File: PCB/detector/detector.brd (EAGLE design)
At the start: 60 x 60 mm, 20 parts, among them U2 B39431B3710U410, U3 LT5537EDDBTRPBF

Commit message: first connection commit
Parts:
- added C10, C11, C12, C13, C14, C15, C18, C22: 100nF, resistor:C0603
- added C16: 1uF, resistor:C0603
- added C17, C19: 4,7uF, rcl:SMC_A
- added C20, C21: 22pF, resistor:C0603
- added CAN+PWR: 4PIN_3.81_KATOWA, zielone raster 3.81:CON-PHOENIX_3.81-4PIN_KAT
- added DA1: SN65HVD230, can_driver:SO08
- added FUSE1: 3A, resistor:R0603
- added IC1: LM50, linear:SOT23
- added L1: 1uH/500mA, rcl:L2012C
- added L2: 10uH/20mA, rcl:L2012C
- added LED1: zielona, led:CHIP-LED0603
- added LED2: niebieska, led:CHIP-LED0603
- added MA_BYC_ACS711_!!: ACS712, acs712:SO08
- added PROGRAMATOR: (no value), pinhead:1X06
- added Q1: (no value), transistor-power:SO-08
- added R10: ZW 0-100K, resistor:R0603
- added R11: 120R*, resistor:R0603
- added R12, R14, R15: 10k, resistor:R0603
- added R13: 820R, resistor:R0603
- added R16: 470R, resistor:R0603
- added R17, R9: 32k, resistor:R0603
- added R2, R4, R5: (no value), rcl:R0603
- added R8: 100K, resistor:R0603
- added SIGNAL1: (no value), adafruit:SMA_EDGELAUNCH
- added TRANSIL1: 3.3V, diode:SMBJ
- added U$2: STM32F072RBT6, STM32F072RBT6:TQFP64
- added U$3: ABM3, crystal_scorpio:ABM3
- added U$4: D24V22F3, przetwornice:D24V22F3
- added U$6: LC03-6R2G, LC03-6R2 - diody ESD do magistrali:SOIC-8
- added ZW_MASY: (no value), resistor:R0603
- added ZW_ZASILANIA: (no value), pinhead:1X02
- moved C1 8.64 mm to (88.6, 5.40)
- moved R1 8.64 mm to (86.1, 4.38)
- moved L3 8.25 mm to (91.4, 4.38)
- moved C2 8.00 mm to (119.2, 5.41)
- moved C4 8.00 mm to (103.3, 5.40)
- moved C5 8.00 mm to (113.6, 5.40)
- moved C7 8.00 mm to (119.2, 3.30)
- moved R7 8.00 mm to (126.1, 6.81)
- moved U$1 8.00 mm to (107.4, 5.14)
- moved U3 8.00 mm to (122.9, 5.16)
- moved C24 8.00 mm to (105.0, 10.8)
- moved C3 8.00 mm to (94.4, 5.40)
- moved C6 8.00 mm to (107.3, 10.8)
- moved L4 8.00 mm to (110.5, 6.35)
- moved R3 8.00 mm to (115.3, 10.2)
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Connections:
- new net +24V: Q1.1, Q1.2, Q1.3, R15.2, U$4.IN+
- new net AGND: C14.2, C16.2, C17.-, C18.2, IC1.3, MA_BYC_ACS711_!!.5, R9.1, U$2.12, ZW_MASY.2
- new net BOOT_0: PROGRAMATOR.4, R14.2, U$2.60
- new net CANH_1: DA1.7, R11.2, U$6.1
- new net CANL_1: DA1.6, R11.1, U$6.4
- new net CAN_RX_1: DA1.4, U$2.61
- new net CAN_TX_1: DA1.1, U$2.62
- new net LED1_ON: U$2.15
- new net LED2_ON: U$2.16
- new net LED3_ON: U$2.17
- new net N$10: MA_BYC_ACS711_!!.1, MA_BYC_ACS711_!!.2, Q1.5, Q1.6, Q1.7, Q1.8
- new net N$12: R13.1, U$2.6
- new net N$13: C20.1, U$2.5, U$3.P$2
- new net N$14: C14.1, C16.1, C17.+, L2.2, U$2.13
- new net N$15: C21.1, R13.2, U$3.P$4
- new net N$16: CAN+PWR.P$2, U$6.8
- new net N$17: CAN+PWR.P$1, U$6.5
- new net N$18: LED1.A, R15.1
- new net N$19: LED2.A, R16.1
- new net N$20: Q1.4, R17.1
- new net N$24: PROGRAMATOR.2, ZW_ZASILANIA.1
- new net N$4: R2.1, SIGNAL.P
- new net N$6: R4.1, SIGNAL1.P
- new net N$7: MA_BYC_ACS711_!!.7, R8.1
- new net N$8: DA1.8, R10.1
- new net N$9: FUSE1.1, U$4.OUT+
- new net NRST: C22.1, PROGRAMATOR.3, U$2.7
- new net OVER_CURRENT: MA_BYC_ACS711_!!.6, R12.2, U$2.2
- new net PRAD_PLYTKI: R8.2, R9.2, U$2.8
- new net SIGNAL1: R2.2, R4.2, R5.2
- new net SWDIO: PROGRAMATOR.6, U$2.46
- new net SWD_CLK: PROGRAMATOR.5, U$2.49
- new net TEMP: IC1.2, U$2.9
- new net VCC: CAN+PWR.P$4, MA_BYC_ACS711_!!.3, MA_BYC_ACS711_!!.4
- new net VDD: C10.1, C11.1, C12.1, C13.1, C15.2, C18.1, C19.+, DA1.3, IC1.1, L1.1, L2.1, MA_BYC_ACS711_!!.8, R12.1, U$2.19, U$2.32, U$2.48, U$2.64, ZW_ZASILANIA.2
- net +3V3: now also FUSE1.2, L1.2, R16.2, TRANSIL1.C
- net GND: now also C10.2, C11.2, C12.2, C13.2, C15.1, C19.-, C20.2, C21.2, C22.2, CAN+PWR.P$3, DA1.2, LED1.C, LED2.C, PROGRAMATOR.1, R10.2, R14.1, R17.2, SIGNAL1.GND@1, SIGNAL1.GND@2, SIGNAL1.GND@3, SIGNAL1.GND@4, TRANSIL1.A, U$2.18, U$2.31, U$2.47, U$2.63, U$3.P$1, U$3.P$3, U$4.GND, U$4.GND1, U$6.2, U$6.3, U$6.6, U$6.7, ZW_MASY.1
- net SIGNAL: now also R5.1; no longer SIGNAL.P
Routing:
- net GND: track 125.9 -> 410.1 mm, vias 98 -> 163
- net VDD: track 0.00 -> 98.7 mm, vias 0 -> 9
- net VCC: track 0.00 -> 43.0 mm
- net AGND: track 0.00 -> 39.5 mm, vias 0 -> 3
- net OVER_CURRENT: track 0.00 -> 27.0 mm, vias 0 -> 2
- net NRST: track 0.00 -> 26.4 mm, vias 0 -> 1
- net N$16: track 0.00 -> 20.9 mm, vias 0 -> 1
- net N$17: track 0.00 -> 20.4 mm
- net PRAD_PLYTKI: track 0.00 -> 17.4 mm
- net TEMP: track 0.00 -> 16.8 mm, vias 0 -> 1
- net +24V: track 0.00 -> 15.8 mm
- net N$9: track 0.00 -> 15.1 mm
- net BOOT_0: track 0.00 -> 14.9 mm, vias 0 -> 2
- net N$6: track 0.00 -> 11.7 mm
- net N$13: track 0.00 -> 10.4 mm
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- removed copper zone on layer 1, net GND
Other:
- board size 60 x 60 mm -> 134.8 x 62.2 mm

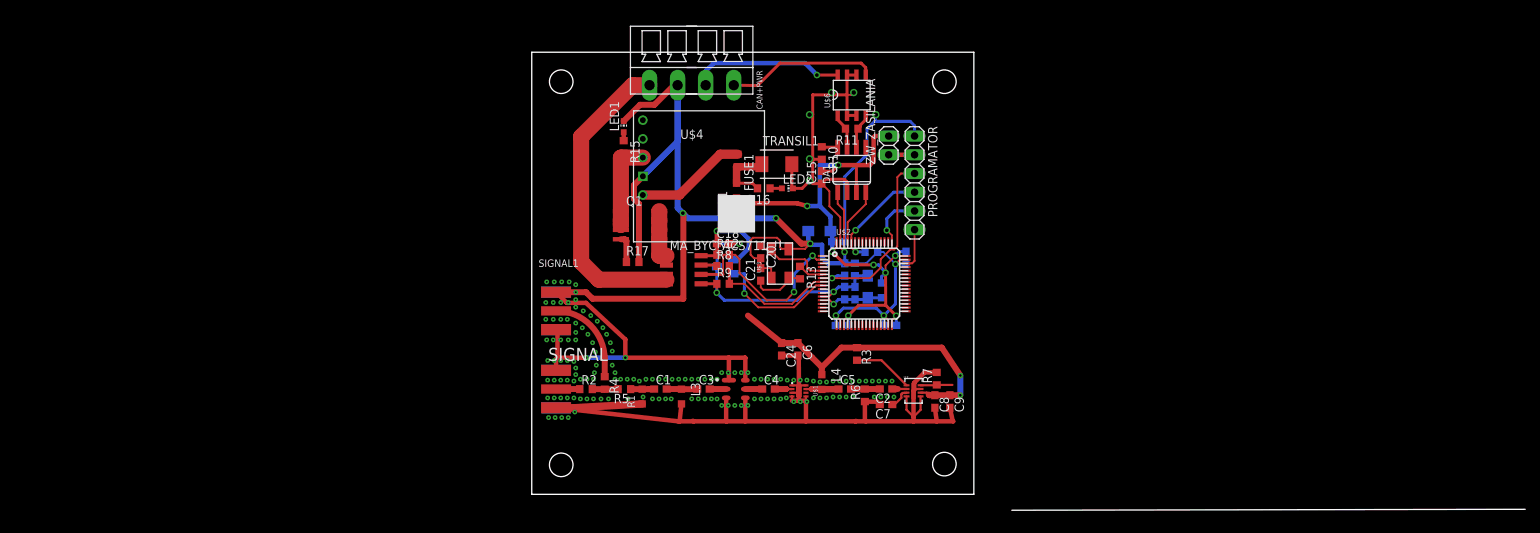
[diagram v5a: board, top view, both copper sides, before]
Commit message: imu added
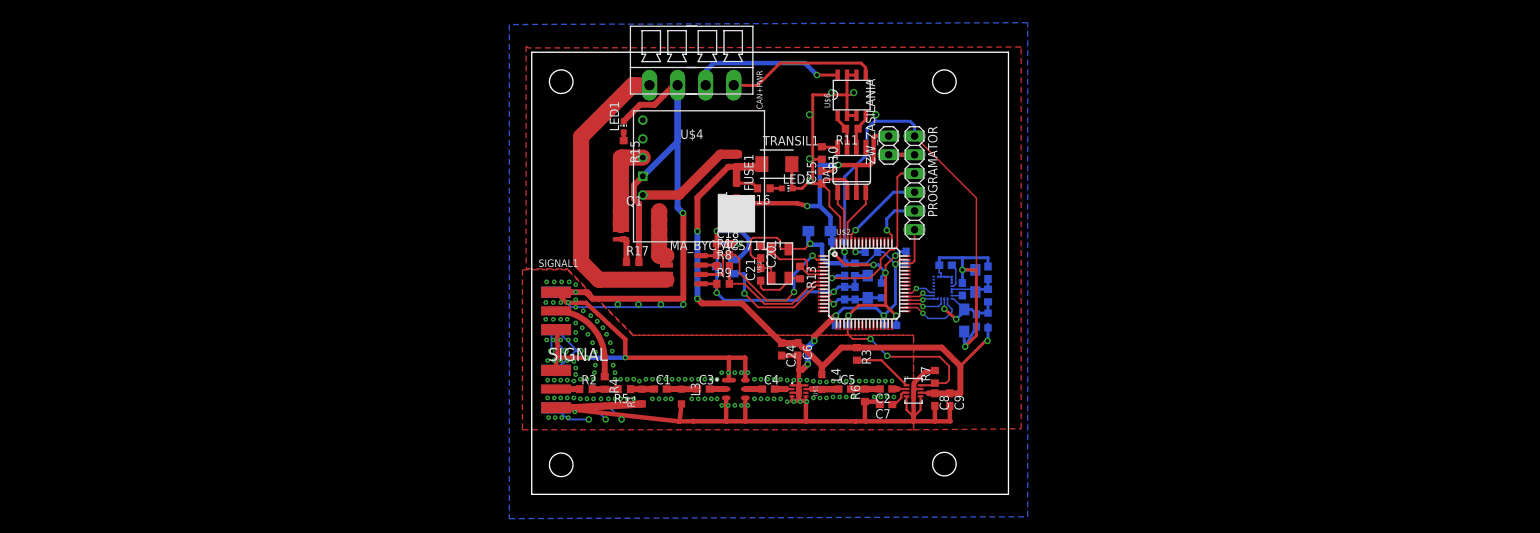
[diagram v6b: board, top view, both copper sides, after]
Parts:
- added C23: 10nF, resistor:C0603
- added C25, C26, C27: 100nF, resistor:C0603
- added C28, C29: 10uF, resistor:SMC_A
- added L5: 10uH, resistor:L2012C
- added R18: 100R, resistor:R0603
- added U$5: LSM9DS1TR, LSM9DS1TR akcelerometr, żyroskop, magnetometr:LGA24
- moved R7 0.36 mm to (125.8, 7.06)
- moved C8 0.25 mm to (125.8, 3.96)
- moved C9 0.25 mm to (127.9, 3.96)
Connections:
- removed net DET_OUT: R7.1, U3.8
- new net CS_AG: U$2.37, U$5.7
- new net CS_M: U$2.38, U$5.8
- new net DEN_AG: U$5.13
- new net DET_ADC: R7.1, U$2.20, U3.8
- new net DRDY_M: U$5.9
- new net INT1_AG: U$5.11
- new net INT2_AG: U$5.12
- new net INT_M: U$5.10
- new net N$21: C27.1, C28.+, R18.2, U$5.22, U$5.23
- new net N$22: C23.1, U$5.21
- new net N$23: C26.1, U$5.24
- new net N$25: C25.2, C29.+, L5.2, R18.1, U$5.1, U$5.3
- new net SCK: U$2.34, U$5.2
- new net SDI: U$2.35, U$5.4
- new net SDO: U$2.36, U$5.5, U$5.6
- net +3V3: now also L5.1
- net GND: now also C23.2, C25.1, C26.2, C27.2, C28.-, C29.-, U$5.14, U$5.15, U$5.16, U$5.17, U$5.18, U$5.19, U$5.20
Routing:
- net GND: track 410.1 -> 520.1 mm, vias 163 -> 178
- net +3V3: track 53.1 -> 89.4 mm, vias 2 -> 3
- net DET_ADC: track 0.00 -> 23.2 mm, vias 0 -> 2
- net N$25: track 0.00 -> 12.7 mm, vias 0 -> 2
- net SCK: track 0.00 -> 9.22 mm, vias 0 -> 1
- net N$21: track 0.00 -> 7.49 mm
- net SDI: track 0.00 -> 5.75 mm, vias 0 -> 1
- net SDO: track 0.00 -> 4.40 mm, vias 0 -> 1
- net DET_OUT: track 4.35 -> 0.00 mm
- net CS_M: track 0.00 -> 4.20 mm, vias 0 -> 1
- net CS_AG: track 0.00 -> 4.06 mm, vias 0 -> 1
- net N$22: track 0.00 -> 3.44 mm
- net N$23: track 0.00 -> 1.45 mm
- added copper zone on layer 1, net GND
- added copper zone on layer 16, net GND
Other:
- board size 134.8 x 62.2 mm -> 64.7 x 60 mm
